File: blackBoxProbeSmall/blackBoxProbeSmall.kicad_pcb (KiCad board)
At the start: 4 copper layers, 44 x 44 mm, 78 parts, among them J1 USB-ID, J2 JTAG_2X05, J3 JTAG_2X05, J4 Conn_01x04, Q1 Q_NMOS_DUAL, Q2 Q_PMOS_DUAL, U1 MCP1702-MB, U2 USBLC6-2, U3 STM32F103CBT, U4 74X2T45, U5 74X2T45, U6 74X2T45, U7 74X2T45, Y1 8.000MHz

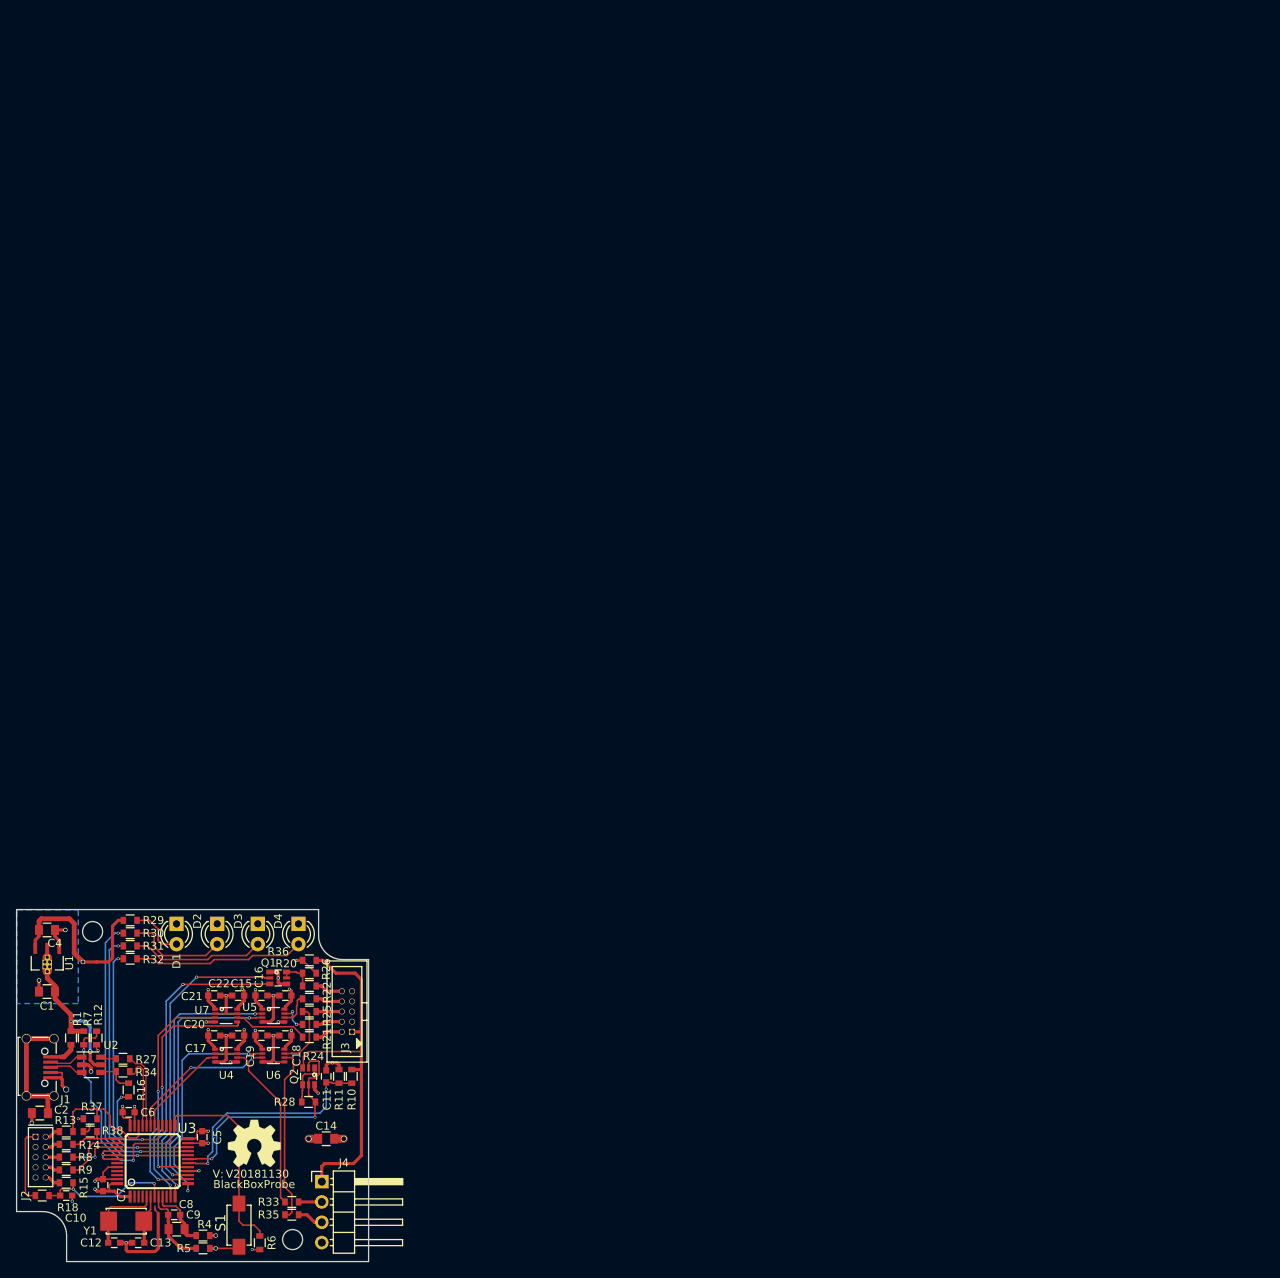
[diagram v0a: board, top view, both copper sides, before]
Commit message: schematic conversion done, started placement of components
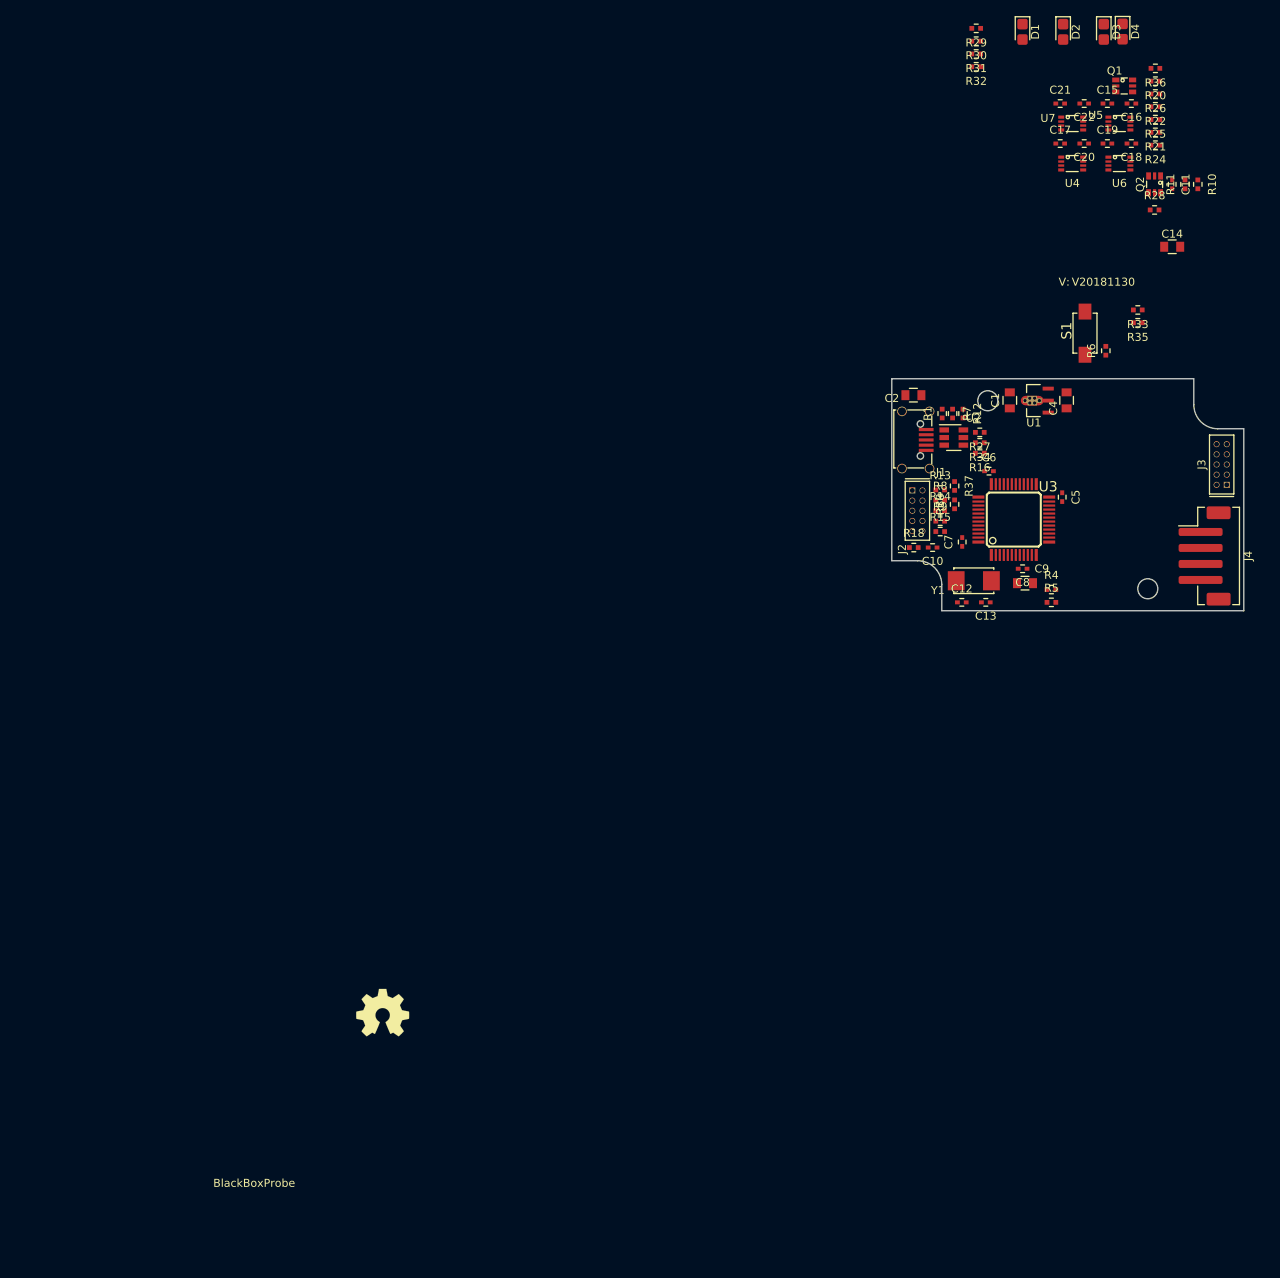
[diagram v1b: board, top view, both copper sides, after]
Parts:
- C10, C11, C12, C13, C15, C16, C17, C18, C19, C20, C21, C22, C5, C6, C7, C8: footprint SquantorRcl:C_0603 -> SquantorRcl:C_0402
- D1, D2, D3, D4: footprint LEDs:LED_D3.0mm -> LED_SMD:LED_0805_2012Metric_Castellated
- J3: footprint SquantorConnectors:Header-Shr-0127-2X05-H006 -> SquantorConnectors:Header-0127-2X05-H006
- J4: footprint Pin_Headers:Pin_Header_Angled_1x04_Pitch2.54mm -> Connector_JST:JST_PH_B4B-PH-SM4-TB_1x04-1MP_P2.00mm_Vertical
- R1, R10, R11, R12, R13, R14, R15, R16, R18, R20, R21, R22, R24, R25, R26, R27, R28, R29, R30, R31, R32, R33, R34, R35, R36, R37, R38, R4, R5, R6, R7, R8, R9: footprint SquantorRcl:R_0603_hand -> SquantorRcl:R_0402_hand
- moved C11 153.7 mm to (158.8, 60.6)
- moved C14 153.7 mm to (158.8, 68.4)
- moved C15 153.7 mm to (150.7, 50.5)
- moved C16 153.7 mm to (153.7, 50.5)
- moved C17 153.7 mm to (144.8, 55.5)
- moved C18 153.7 mm to (153.7, 55.5)
- moved C19 153.7 mm to (150.7, 55.5)
- moved C20 153.7 mm to (147.8, 55.5)
- moved C21 153.7 mm to (144.8, 50.5)
- moved C22 153.7 mm to (147.8, 50.5)
- moved D1 153.7 mm to (140.0, 41.5)
- moved D2 153.7 mm to (145.1, 41.5)
- moved D3 153.7 mm to (150.2, 41.5)
- moved N2 153.7 mm to (150.2, 72.9)
- moved Q1 153.7 mm to (152.8, 48.3)
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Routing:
- net GND: track 81.7 -> 0.00 mm, vias 21 -> 0
- net +3V3: track 70.7 -> 0.00 mm, vias 16 -> 0
- net /PROBE_VDD: track 47.5 -> 0.00 mm
- net /PROBE_I_RST: track 39.2 -> 0.00 mm, vias 2 -> 0
- net /PROBE_I_RST_SEN: track 38.7 -> 0.00 mm, vias 2 -> 0
- net /LED0: track 38.5 -> 0.00 mm, vias 2 -> 0
- net /PROBE_E_VDD: track 38.1 -> 0.00 mm, vias 5 -> 0
- net /LED1: track 35.9 -> 0.00 mm, vias 2 -> 0
- net /PROBE_I_TDI: track 34.0 -> 0.00 mm, vias 2 -> 0
- net /PROBE_I_TCK: track 33.3 -> 0.00 mm, vias 2 -> 0
- net /LED2: track 33.1 -> 0.00 mm, vias 2 -> 0
- net /PROBE_TMS_DIR: track 31.7 -> 0.00 mm, vias 2 -> 0
- net /PROBE_I_TMS: track 30.5 -> 0.00 mm, vias 2 -> 0
- net /TARGET_PWR_EN: track 30.2 -> 0.00 mm, vias 2 -> 0
- net /USB_V: track 29.8 -> 0.00 mm, vias 2 -> 0
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- removed copper zone on In2.Cu, net +3V3
- removed copper zone on B.Cu, net +5V
- removed copper zone on In1.Cu, net GND
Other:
- board size 44 x 44 mm -> 44 x 29 mm

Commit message: small updates in placement
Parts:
- C1: value 2.2u -> 1u; footprint SquantorRcl:C_0805 -> SquantorRcl:C_0603
- moved R30 47.0 mm to (147.9, 87.7)
- moved R31 47.0 mm to (147.9, 89.3)
- moved R29 47.0 mm to (147.9, 86.1)
- moved R32 47.0 mm to (147.9, 90.9)
- moved D4 6.55 mm to (146.0, 41.6)
- moved D3 6.20 mm to (144.0, 41.5)
- moved D2 3.12 mm to (142.0, 41.5)
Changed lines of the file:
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@@
     (add_net VDDA)
+  )
+  (module SquantorIC:SOT89-ViaTab-Microchip-MB (layer F.Cu)
+    (at 143.25 87.63 90)
+    (fp_text reference U1 (at -2.77 -1.8 180) (layer F.SilkS)
+      (effects (font (size 1 1) (thickness 0.15)))
+    )
+    (fp_text value MCP1702-MB (at 0 2 90) (layer F.Fab)
+      (effects (font (size 1 1) (thickness 0.15)))
+    )
+    (fp_line (start 2 -2.7) (end 2 -1) (layer F.SilkS) (width 0.15))
+    (fp_line (start 1.2 -2.7) (end 2 -2.7) (layer F.SilkS) (width 0.15))
+    (fp_line (start -2 -2.7) (end -1.2 -2.7) (layer F.SilkS) (width 0.15))
+    (fp_line (start -2 -1) (end -2 -2.7) (layer F.SilkS) (width 0.15))
+    (pad 1 smd rect (at -1.5 0 90) (size 0.7 1.4) (layers F.Cu F.Paste F.Mask)
+      (net 2 GND))
+    (pad 2 smd rect (at 0 0 90) (size 0.7 1.4) (layers F.Cu F.Paste F.Mask)
+      (net 1 +5V))
+    (pad 3 smd rect (at 1.5 0 90) (size 0.7 1.4) (layers F.Cu F.Paste F.Mask)
+      (net 4 +3V3))
+    (pad TAB smd oval (at 0 -2.1 90) (size 2 3.05) (layers F.Cu F.Paste F.Mask)
+      (net 1 +5V) (zone_connect 2))
+    (pad TAB thru_hole rect (at -0.3 -1.7 90) (size 0.6 0.6) (drill 0.4) (layers *.Cu *.Mask)
+      (net 1 +5V) (zone_connect 2))
+    (pad TAB thru_hole rect (at 0.3 -1.7 90) (size 0.6 0.6) (drill 0.4) (layers *.Cu *.Mask)
+      (net 1 +5V) (zone_connect 2))
+    (pad TAB thru_hole rect (at 0.3 -2.3 90) (size 0.6 0.6) (drill 0.4) (layers *.Cu *.Mask)
+      (net 1 +5V) (zone_connect 2))
+    (pad TAB thru_hole rect (at -0.3 -2.3 90) (size 0.6 0.6) (drill 0.4) (layers *.Cu *.Mask)
+      (net 1 +5V) (zone_connect 2))
+    (pad TAB thru_hole rect (at 0 -2.9 90) (size 0.6 0.6) (drill 0.4) (layers *.Cu *.Mask)
+      (net 1 +5V) (zone_connect 2))
+    (pad TAB thru_hole rect (at 0 -1.1 90) (size 0.6 0.6) (drill 0.4) (layers *.Cu *.Mask)
+      (net 1 +5V) (zone_connect 2))
   )
   (module SquantorConnectors:Header-0127-2X05-H006 (layer F.Cu)
@@
   )
   (module SquantorRcl:C_0805 (layer F.Cu)
-    (at 138.45 87.6 90)
-    (descr "Capacitor SMD 0805, reflow soldering, AVX (see smccp.pdf)")
-    (tags "capacitor 0805")
-    (attr smd)
-    (fp_text reference C1 (at 0 -1.8 90) (layer F.SilkS)
-      (effects (font (size 1 1) (thickness 0.15)))
-    )
-    (fp_text value 2.2u (at -6.35 0.1 90) (layer F.Fab)
-      (effects (font (size 1 1) (thickness 0.15)))
-    )
-    (fp_line (start -1 0.625) (end -1 -0.625) (layer F.Fab) (width 0.15))
-    (fp_line (start 1 0.625) (end -1 0.625) (layer F.Fab) (width 0.15))
-    (fp_line (start 1 -0.625) (end 1 0.625) (layer F.Fab) (width 0.15))
-    (fp_line (start -1 -0.625) (end 1 -0.625) (layer F.Fab) (width 0.15))
-    (fp_line (start -1.8 -1) (end 1.8 -1) (layer F.CrtYd) (width 0.05))
-    (fp_line (start -1.8 1) (end 1.8 1) (layer F.CrtYd) (width 0.05))
-    (fp_line (start -1.8 -1) (end -1.8 1) (layer F.CrtYd) (width 0.05))
-    (fp_line (start 1.8 -1) (end 1.8 1) (layer F.CrtYd) (width 0.05))
-    (fp_line (start 0.5 -0.85) (end -0.5 -0.85) (layer F.SilkS) (width 0.15))
-    (fp_line (start -0.5 0.85) (end 0.5 0.85) (layer F.SilkS) (width 0.15))
-    (pad 1 smd rect (at -1 0 90) (size 1 1.25) (layers F.Cu F.Paste F.Mask)
-      (net 1 +5V))
-    (pad 2 smd rect (at 1 0 90) (size 1 1.25) (layers F.Cu F.Paste F.Mask)
-      (net 2 GND))
-    (model Capacitors_SMD.3dshapes/C_0805.wrl
-      (at (xyz 0 0 0))
-      (scale (xyz 1 1 1))
-      (rotate (xyz 0 0 0))
-    )
-  )
-  (module SquantorRcl:C_0805 (layer F.Cu)
     (at 126.4 86.95 180)
     (descr "Capacitor SMD 0805, reflow soldering, AVX (see smccp.pdf)")
@@
       (net 63 /PROBE_E_VDD))
   )
-  (module SquantorIC:SOT89-ViaTab-Microchip-MB (layer F.Cu)
-    (at 143.25 87.63 90)
-    (fp_text reference U1 (at -2.77 -1.8 180) (layer F.SilkS)
-      (effects (font (size 1 1) (thickness 0.15)))
-    )
-    (fp_text value MCP1702-MB (at 0 2 90) (layer F.Fab)
-      (effects (font (size 1 1) (thickness 0.15)))
-    )
-    (fp_line (start 2 -2.7) (end 2 -1) (layer F.SilkS) (width 0.15))
-    (fp_line (start 1 -2.7) (end 2 -2.7) (layer F.SilkS) (width 0.15))
-    (fp_line (start -2 -2.7) (end -1 -2.7) (layer F.SilkS) (width 0.15))
-    (fp_line (start -2 -1) (end -2 -2.7) (layer F.SilkS) (width 0.15))
-    (pad 1 smd rect (at -1.5 0 90) (size 0.48 1.4) (layers F.Cu F.Paste F.Mask)
-      (net 2 GND))
-    (pad 2 smd rect (at 0 0 90) (size 0.48 1.4) (layers F.Cu F.Paste F.Mask)
-      (net 1 +5V))
-    (pad 3 smd rect (at 1.5 0 90) (size 0.48 1.4) (layers F.Cu F.Paste F.Mask)
-      (net 4 +3V3))
-    (pad TAB smd oval (at 0 -2 90) (size 1.2 2.85) (layers F.Cu F.Paste F.Mask)
-      (net 1 +5V) (zone_connect 2))
-    (pad TAB thru_hole rect (at -0.3 -1.7 90) (size 0.6 0.6) (drill 0.4) (layers *.Cu *.Mask)
-      (net 1 +5V) (zone_connect 2))
-    (pad TAB thru_hole rect (at 0.3 -1.7 90) (size 0.6 0.6) (drill 0.4) (layers *.Cu *.Mask)
-      (net 1 +5V) (zone_connect 2))
-    (pad TAB thru_hole rect (at 0.3 -2.3 90) (size 0.6 0.6) (drill 0.4) (layers *.Cu *.Mask)
-      (net 1 +5V) (zone_connect 2))
-    (pad TAB thru_hole rect (at -0.3 -2.3 90) (size 0.6 0.6) (drill 0.4) (layers *.Cu *.Mask)
-      (net 1 +5V) (zone_connect 2))
-    (pad TAB thru_hole rect (at 0 -2.9 90) (size 0.6 0.6) (drill 0.4) (layers *.Cu *.Mask)
-      (net 1 +5V) (zone_connect 2))
-    (pad TAB thru_hole rect (at 0 -1.1 90) (size 0.6 0.6) (drill 0.4) (layers *.Cu *.Mask)
-      (net 1 +5V) (zone_connect 2))
-  )
   (module SquantorRcl:C_0402 (layer F.Cu)
     (at 145 99.7 270)
@@
   )
   (module SquantorRcl:R_0402_hand (layer F.Cu)
-    (at 134.25 41.1 180)
+    (at 147.95 86.1 180)
     (descr "Resistor SMD 0402, reflow soldering, Vishay (see dcrcw.pdf)")
     (tags "resistor 0402")
@@
   )
   (module SquantorRcl:R_0402_hand (layer F.Cu)
-    (at 134.25 42.7 180)
+    (at 147.95 87.7 180)
     (descr "Resistor SMD 0402, reflow soldering, Vishay (see dcrcw.pdf)")
     (tags "resistor 0402")
@@
   )
   (module SquantorRcl:R_0402_hand (layer F.Cu)
-    (at 134.25 44.3 180)
+    (at 147.95 89.3 180)
     (descr "Resistor SMD 0402, reflow soldering, Vishay (see dcrcw.pdf)")
     (tags "resistor 0402")
@@
   )
   (module SquantorRcl:R_0402_hand (layer F.Cu)
-    (at 134.25 45.9 180)
+    (at 147.95 90.9 180)
     (descr "Resistor SMD 0402, reflow soldering, Vishay (see dcrcw.pdf)")
     (tags "resistor 0402")
@@
   )
   (module LED_SMD:LED_0805_2012Metric_Castellated (layer F.Cu)
-    (at 145.12 41.535 270)
+    (at 142 41.535 270)
     (descr "LED SMD 0805 (2012 Metric), castellated end terminal, IPC_7351 nominal, (Body size source: https://docs.google.com/spreadsheets/d/1BsfQQcO9C6DZCsRaXUlFlo91Tg2WpOkGARC1WS5S8t0/edit?usp=sharing), generated with kicad-footprint-generator")
     (tags "LED castellated")
@@
   )
   (module LED_SMD:LED_0805_2012Metric_Castellated (layer F.Cu)
-    (at 150.2 41.535 270)
+    (at 144 41.535 270)
     (descr "LED SMD 0805 (2012 Metric), castellated end terminal, IPC_7351 nominal, (Body size source: https://docs.google.com/spreadsheets/d/1BsfQQcO9C6DZCsRaXUlFlo91Tg2WpOkGARC1WS5S8t0/edit?usp=sharing), generated with kicad-footprint-generator")
     (tags "LED castellated")
@@
   )
   (module LED_SMD:LED_0805_2012Metric_Castellated (layer F.Cu)
-    (at 152.55 41.5 270)
+    (at 146 41.6 270)
     (descr "LED SMD 0805 (2012 Metric), castellated end terminal, IPC_7351 nominal, (Body size source: https://docs.google.com/spreadsheets/d/1BsfQQcO9C6DZCsRaXUlFlo91Tg2WpOkGARC1WS5S8t0/edit?usp=sharing), generated with kicad-footprint-generator")
     (tags "LED castellated")
@@
       (at (xyz 0 0 0))
       (scale (xyz 1 1 1))
+      (rotate (xyz 0 0 0))
+    )
+  )
+  (module SquantorRcl:C_0603 (layer F.Cu)
+    (at 138.45 87.6 90)
+    (descr "Capacitor SMD 0603, reflow soldering, AVX (see smccp.pdf)")
+    (tags "capacitor 0603")
+    (attr smd)
+    (fp_text reference C1 (at 0 -1.9 90) (layer F.SilkS)
+      (effects (font (size 1 1) (thickness 0.15)))
+    )
+    (fp_text value 1u (at 0 1.9 90) (layer F.Fab)
+      (effects (font (size 1 1) (thickness 0.15)))
+    )
+    (fp_line (start -0.8 0.4) (end -0.8 -0.4) (layer F.Fab) (width 0.15))
+    (fp_line (start 0.8 0.4) (end -0.8 0.4) (layer F.Fab) (width 0.15))
+    (fp_line (start 0.8 -0.4) (end 0.8 0.4) (layer F.Fab) (width 0.15))
+    (fp_line (start -0.8 -0.4) (end 0.8 -0.4) (layer F.Fab) (width 0.15))
+    (fp_line (start -1.45 -0.75) (end 1.45 -0.75) (layer F.CrtYd) (width 0.05))
+    (fp_line (start -1.45 0.75) (end 1.45 0.75) (layer F.CrtYd) (width 0.05))
+    (fp_line (start -1.45 -0.75) (end -1.45 0.75) (layer F.CrtYd) (width 0.05))
+    (fp_line (start 1.45 -0.75) (end 1.45 0.75) (layer F.CrtYd) (width 0.05))
+    (fp_line (start -0.35 -0.6) (end 0.35 -0.6) (layer F.SilkS) (width 0.15))
+    (fp_line (start 0.35 0.6) (end -0.35 0.6) (layer F.SilkS) (width 0.15))
+    (pad 1 smd rect (at -0.75 0 90) (size 0.8 0.75) (layers F.Cu F.Paste F.Mask)
+      (net 1 +5V))
+    (pad 2 smd rect (at 0.75 0 90) (size 0.8 0.75) (layers F.Cu F.Paste F.Mask)
+      (net 2 GND))
+    (model Capacitors_SMD.3dshapes/C_0603.wrl
+      (at (xyz 0 0 0))
+      (scale (xyz 1 1 1))

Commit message: further placement of components, everything fits on pcb, now compacting due to smaller footprints
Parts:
- removed D1: Green, LED_SMD:LED_0805_2012Metric_Castellated
- removed D2: Yellow, LED_SMD:LED_0805_2012Metric_Castellated
- removed D3: Orange, LED_SMD:LED_0805_2012Metric_Castellated
- removed D4: Red, LED_SMD:LED_0805_2012Metric_Castellated
- removed N3: BlackBoxProbe, SquantorLabels:Label_version
- added DA1: mentor_1296.4124, SquantorOpto:mentor_1296.4124, F.Cu at (155.5, 88.5)
- J4: footprint Connector_JST:JST_PH_B4B-PH-SM4-TB_1x04-1MP_P2.00mm_Vertical -> Connector_JST:JST_PH_S4B-PH-K_1x04_P2.00mm_Horizontal
- moved N1 108.4 mm to (141.6, 92.7)
- moved Q1 56.5 mm to (158.9, 104.5)
- moved R20 46.5 mm to (161.6, 93.9)
- moved R24 46.5 mm to (161.6, 101.9)
- moved R25 46.5 mm to (161.6, 98.7)
- moved R26 46.5 mm to (161.6, 95.5)
- moved R21 46.5 mm to (161.6, 100.3)
- moved R22 46.5 mm to (161.6, 97.1)
- moved R36 46.5 mm to (161.6, 92.3)
- moved R10 46.0 mm to (151.2, 105.3)
- moved R11 46.0 mm to (149.7, 105.3)
- moved C11 45.9 mm to (148.4, 105.3)
- moved R28 44.0 mm to (154.9, 107.8)
- moved Q2 44.0 mm to (154.9, 104.6)
- moved C21 42.8 mm to (151.4, 92.8)
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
